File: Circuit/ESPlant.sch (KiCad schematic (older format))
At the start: 32 parts, among them P101 CONN_01X08, P102 CONN_01X08, P103 SOLAR, P104 USB_5PIN_SHELL, P105 CONN_01X05, Q101 FDN340P, SW101 RESET, SW102 PRGM, SW103 RESET, U101 STM32F042F, U102 ESP-12E

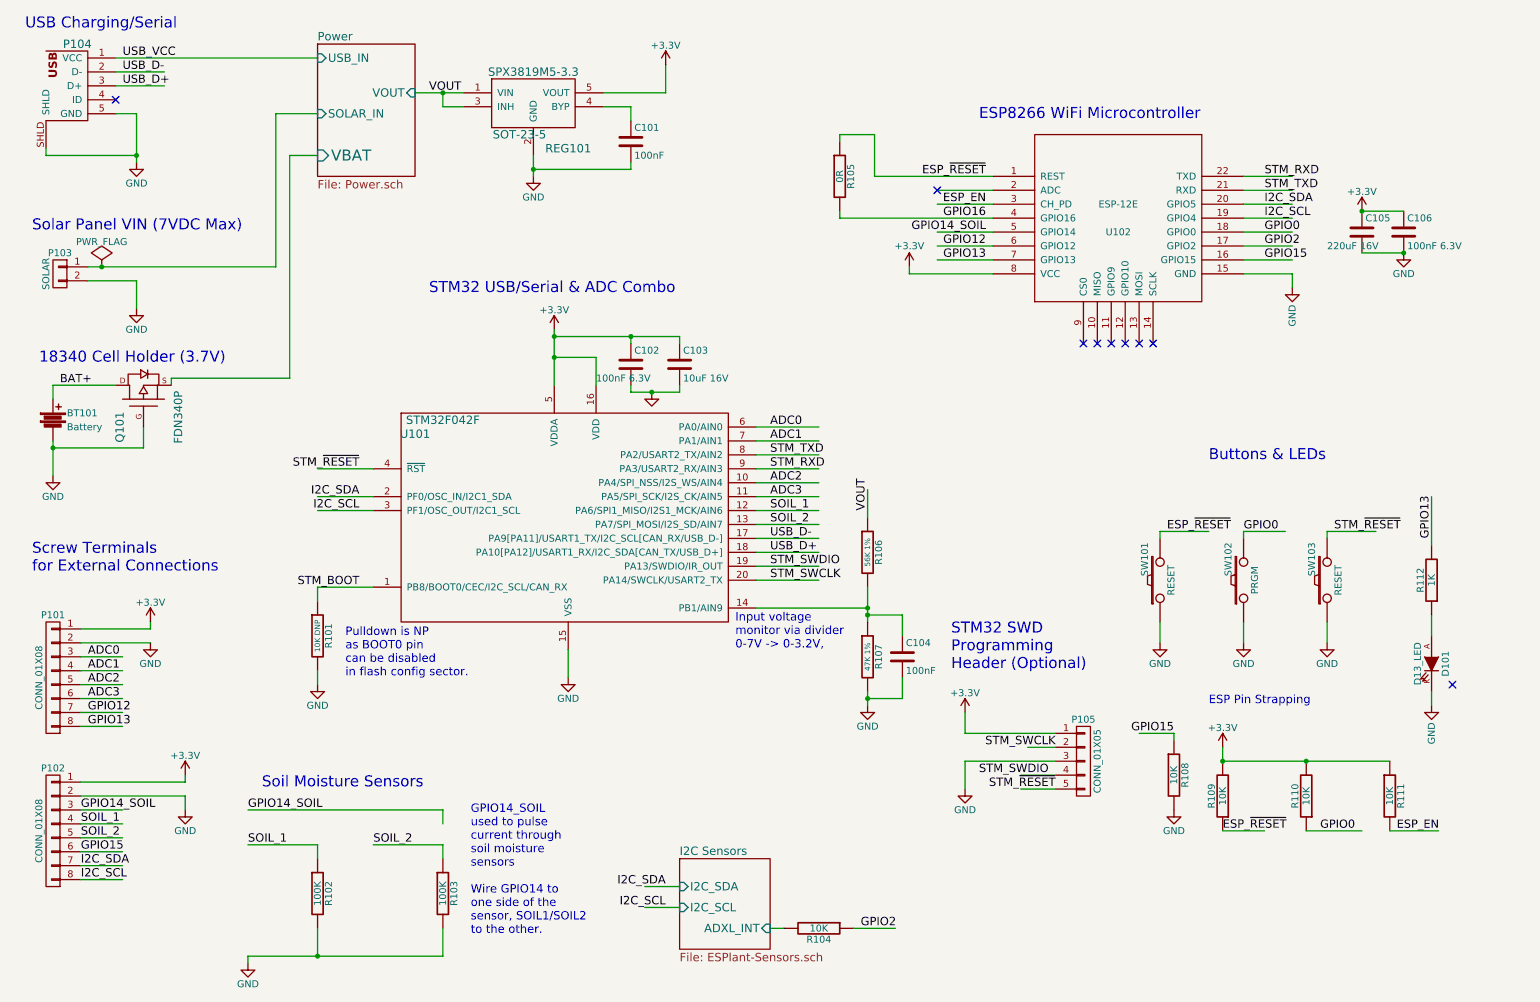
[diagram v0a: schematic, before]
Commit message: Schematic last touches
Added:
Breakouts for individual sensors.
Breakouts for all pins.
ESP controllable power.
Replaced Battery FET with Fuse.
Removed D13 LED.
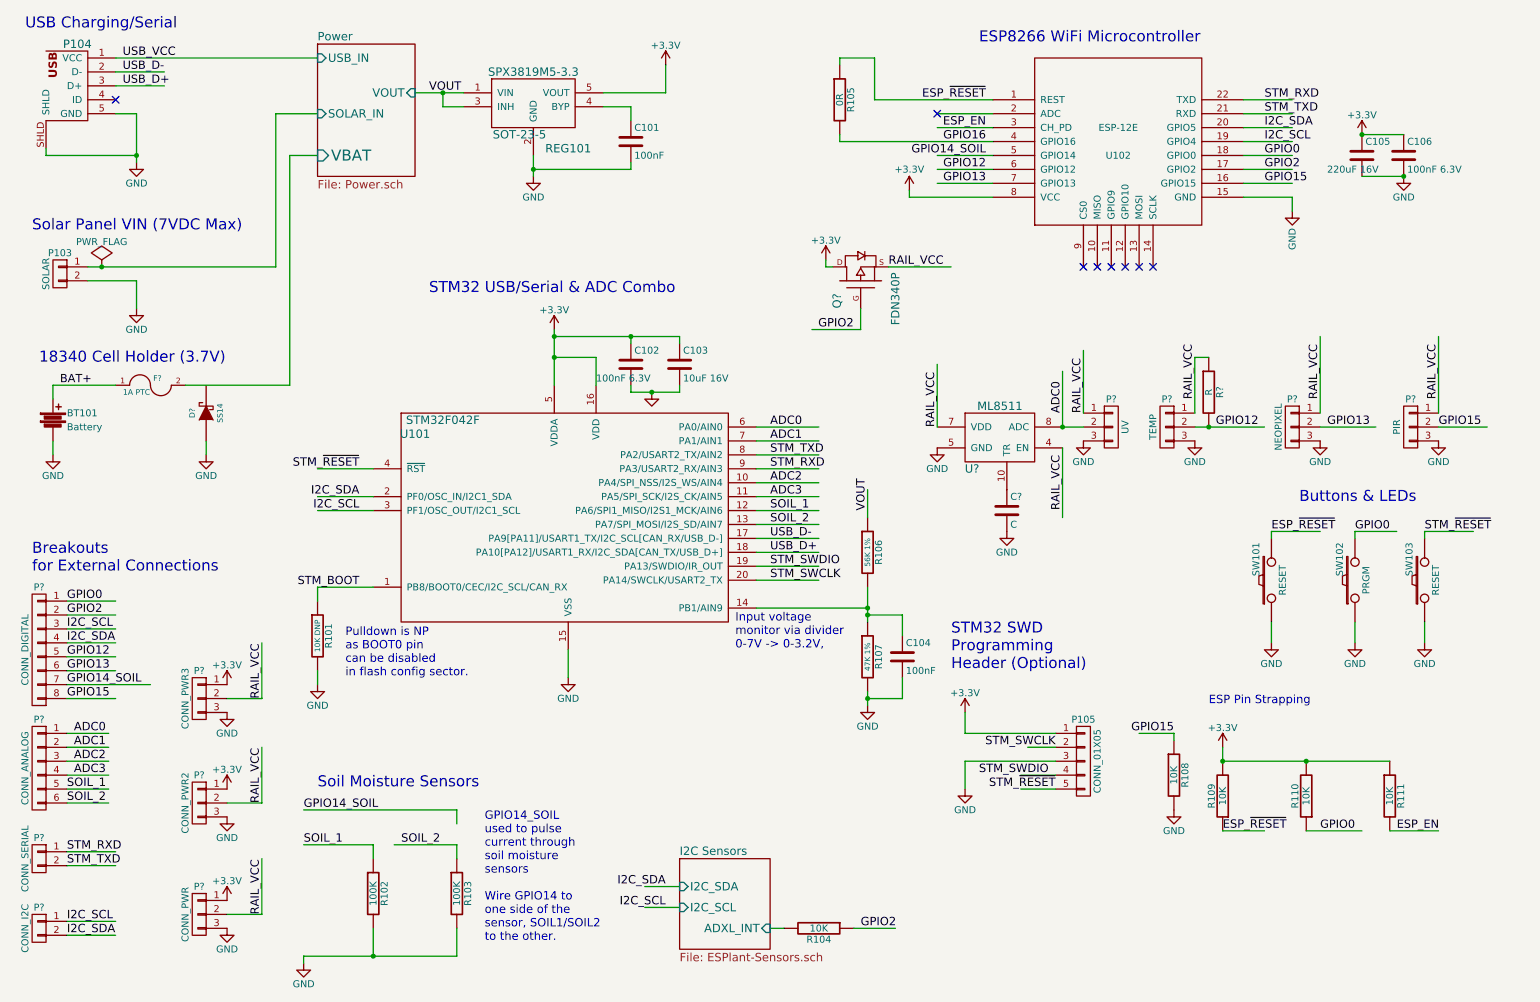
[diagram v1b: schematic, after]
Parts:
- removed D101: D13_LED, symbol LED
- removed P101, P102: CONN_01X08, symbol CONN_01X08
- removed Q101: FDN340P, symbol MOSFET_P
- removed R112: 1K, symbol R
- added C?: C, symbol C
- added D?: SS14, symbol DIODE_SCHOTTKY
- added F?: 1A PTC, symbol FUSE
- added P?: UV, symbol CONN_01X03
- added P?: PIR, symbol CONN_01X03
- added P?: TEMP, symbol CONN_01X03
- added P?: NEOPIXEL, symbol CONN_01X03
- added P?: CONN_PWR, symbol CONN_01X03
- added P?: CONN_ANALOG, symbol CONN_01X06
- added P?: CONN_SERIAL, symbol CONN_01X02
- added P?: CONN_DIGITAL, symbol CONN_01X08
- added P?: CONN_I2C, symbol CONN_01X02
- added P?: CONN_PWR3, symbol CONN_01X03
- added P?: CONN_PWR2, symbol CONN_01X03
- added Q?: FDN340P, symbol MOSFET_P
- added R?: R, symbol R
- added U?: ML8511, symbol ML8511
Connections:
- net labels added: RAIL_VCC
- wire segments 151 -> 168
- no-connect marks 9 -> 8
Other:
- note added: "Breakouts\nfor External Connections"
- note removed: "Screw Terminals\nfor External Connections"
- moved on the sheet: C105, C106, R102, R103, R105, SW101, SW102, SW103, U102

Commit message: Rename RAIL_VCC to VCC_SENS, add pullup and gate current resistor to FET
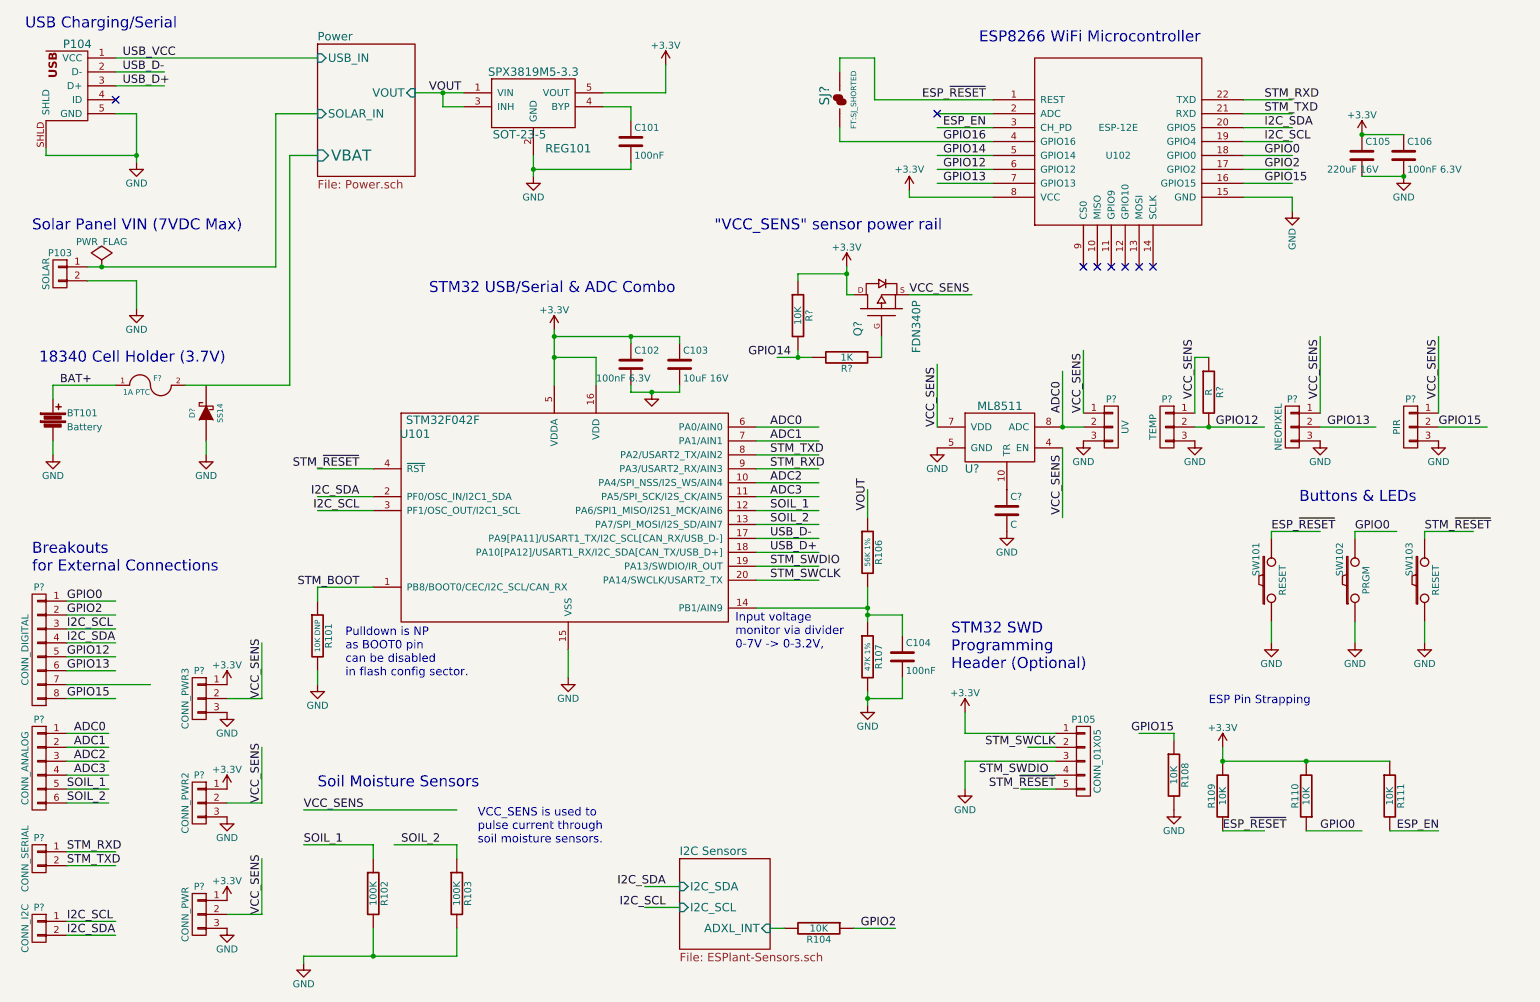
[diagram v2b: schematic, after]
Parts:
- removed R105: 0R, symbol R
- added R?: 10K, symbol R
- added R?: 1K, symbol R
- added SJ?: SJ, FT:SJ_SHORTED, symbol SJ
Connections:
- net labels added: GPIO14, VCC_SENS
- net labels removed: GPIO14_SOIL, RAIL_VCC
- wire segments 168 -> 169
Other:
- note added: ""VCC_SENS" sensor power rail"
- note added: "VCC_SENS is used to\npulse current through\nsoil moisture sensors."
- note removed: "GPIO14_SOIL\nused to pulse\ncurrent through\nsoil moisture\nsensors\n\nWire GPIO14 to\none side of the\nsensor, SOIL1/SOIL2\nto the other."
- moved on the sheet: Q?
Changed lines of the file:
@@
 NoConn ~ 8350 2350
 NoConn ~ 8250 2350
-Text Notes 3950 7200 0    60   ~ 0
-GPIO14_SOIL\nused to pulse\ncurrent through\nsoil moisture\nsensors\n\nWire GPIO14 to\none side of the\nsensor, SOIL1/SOIL2\nto the other.
+Text Notes 3900 6500 0    60   ~ 0
+VCC_SENS is used to\npulse current through\nsoil moisture sensors.
 Text Label 6000 3500 0    60   ~ 0
 ADC0
-$Comp
-L R R105
-U 1 1 564EAB03
-P 6500 1150
-F 0 "R105" V 6580 1150 50  0000 C CNN
-F 1 "0R" V 6500 1150 50  0000 C CNN
-F 2 "" H 6500 1150 60  0000 C CNN
-F 3 "" H 6500 1150 60  0000 C CNN
-	1    6500 1150
-	1    0    0    -1
-$EndComp
 Text Label 7550 1550 2    60   ~ 0
-GPIO14_SOIL
+GPIO14
 Text Label 2650 6250 0    60   ~ 0
-GPIO14_SOIL
+VCC_SENS
 $Comp
 L GND #PWR019
@@
 L MOSFET_P Q?
 U 1 1 565907EF
-P 6650 2450
-F 0 "Q?" H 6560 2620 60  0000 R CNN
-F 1 "FDN340P" H 6710 2200 60  0000 R CNN
-F 2 "" H 6650 2450 60  0000 C CNN
-F 3 "" H 6650 2450 60  0000 C CNN
-	1    6650 2450
+P 6800 2650
+F 0 "Q?" H 6710 2820 60  0000 R CNN
+F 1 "FDN340P" H 6860 2400 60  0000 R CNN
+F 2 "" H 6800 2650 60  0000 C CNN
+F 3 "" H 6800 2650 60  0000 C CNN
+	1    6800 2650
 	0    -1   -1   0
 $EndComp
@@
 L +3.3V #PWR?
 U 1 1 56596CF8
-P 6400 2300
-F 0 "#PWR?" H 6400 2150 50  0001 C CNN
-F 1 "+3.3V" H 6400 2440 50  0000 C CNN
-F 2 "" H 6400 2300 60  0000 C CNN
-F 3 "" H 6400 2300 60  0000 C CNN
-	1    6400 2300
-	1    0    0    -1
-$EndComp
-Text Label 6600 2800 2    60   ~ 0
-GPIO2
-Text Label 6850 2350 0    60   ~ 0
-RAIL_VCC
+P 6550 2350
+F 0 "#PWR?" H 6550 2200 50  0001 C CNN
+F 1 "+3.3V" H 6550 2490 50  0000 C CNN
+F 2 "" H 6550 2350 60  0000 C CNN
+F 3 "" H 6550 2350 60  0000 C CNN
+	1    6550 2350
+	1    0    0    -1
+$EndComp
+Text Label 7000 2550 0    60   ~ 0
+VCC_SENS
 Text Label 7200 3500 1    60   ~ 0
-RAIL_VCC
+VCC_SENS
 Text Label 8100 3700 3    60   ~ 0
-RAIL_VCC
+VCC_SENS
 Text Label 9050 3300 1    60   ~ 0
-RAIL_VCC
+VCC_SENS
 Text Label 8250 3400 1    60   ~ 0
-RAIL_VCC
+VCC_SENS
 Text Label 9950 3300 1    60   ~ 0
-RAIL_VCC
+VCC_SENS
 Text Label 10800 3300 1    60   ~ 0
-RAIL_VCC
+VCC_SENS
 Wire Wire Line
 	3750 6500 3300 6500
@@
 	7200 3500 7200 3050
 Wire Wire Line
-	6400 2350 6450 2350
-Wire Wire Line
-	6400 2300 6400 2350
-Wire Wire Line
-	6650 2800 6300 2800
-Wire Wire Line
-	6650 2650 6650 2800
-Wire Wire Line
-	6850 2350 7300 2350
+	6550 2550 6600 2550
+Wire Wire Line
+	6550 2350 6550 2550
+Wire Wire Line
+	6800 3000 6800 2850
+Wire Wire Line
+	7000 2550 7450 2550
 Wire Wire Line
 	9050 3500 9550 3500
@@
 	2650 6500 3150 6500
 Wire Wire Line
-	3750 6250 3750 6350
-Wire Wire Line
 	2650 6250 3750 6250
 Wire Wire Line
-	6750 1450 6750 1450
-Wire Wire Line
-	6500 1400 6500 1450
-Wire Wire Line
-	6500 850  6500 900
+	6500 1350 6500 1450
+Wire Wire Line
+	6500 850  6500 950
 Wire Wire Line
 	6750 850  6500 850
@@
 	10450 6400 10800 6400
 Connection ~ 9850 5900
-Wire Wire Line
-	6500 1450 7600 1450
 Wire Wire Line
 	7600 1650 7200 1650
@@
 Text Label 950  5150 0    60   ~ 0
 GPIO12
-Text Label 950  5350 0    60   ~ 0
-GPIO14_SOIL
 $Comp
 L CONN_01X03 P?
@@
 $EndComp
 Text Label 2350 7000 1    60   ~ 0
-RAIL_VCC
+VCC_SENS
 $Comp
 L CONN_01X06 P?
@@
 $EndComp
 Text Label 2350 5450 1    60   ~ 0
-RAIL_VCC
+VCC_SENS
 Wire Wire Line
 	2100 5450 2350 5450
@@
 $EndComp
 Text Label 2350 6200 1    60   ~ 0
-RAIL_VCC
+VCC_SENS
 Wire Wire Line
 	2100 6200 2350 6200
@@
 Wire Wire Line
 	1950 3600 1950 3700
+$Comp
+L SJ SJ?
+U 1 1 56581F55
+P 6500 1150
+F 0 "SJ?" H 6400 1000 70  0000 L BNN
+F 1 "SJ" H 6400 1200 30  0001 L BNN
+F 2 "FT:SJ_SHORTED" H 6500 1250 39  0000 C CNN
+F 3 "" H 6500 1150 60  0000 C CNN
+	1    6500 1150
+	0    1    1    0
+$EndComp
+Wire Wire Line
+	6500 1450 7600 1450
+Text Label 6150 3000 2    60   ~ 0
+GPIO14
+$Comp
+L R R?
+U 1 1 56584EA4
+P 6200 2700
+F 0 "R?" V 6280 2700 50  0000 C CNN
+F 1 "10K" V 6200 2700 50  0000 C CNN
+F 2 "" H 6200 2700 60  0000 C CNN
+F 3 "" H 6200 2700 60  0000 C CNN
+	1    6200 2700
+	1    0    0    -1
+$EndComp
+Connection ~ 6200 3000
+Wire Wire Line
+	6200 2400 6550 2400
+Connection ~ 6550 2400
+$Comp
+L R R?
+U 1 1 56585798
+P 6550 3000
+F 0 "R?" V 6630 3000 50  0000 C CNN
+F 1 "1K" V 6550 3000 50  0000 C CNN
+F 2 "" H 6550 3000 60  0000 C CNN
+F 3 "" H 6550 3000 60  0000 C CNN
+	1    6550 3000
+	0    1    1    0
+$EndComp
+Wire Wire Line
+	6050 3000 6300 3000
+Wire Wire Line
+	6200 3000 6200 2950
+Wire Wire Line
+	6200 2450 6200 2400
+Text Notes 5600 2100 0    79   ~ 0
+"VCC_SENS" sensor power rail
 $EndSCHEMATC

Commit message: Footprint assignment for schematic, including footprints for new parts
Removed on-PCB UV sensor in favour of offboard one.
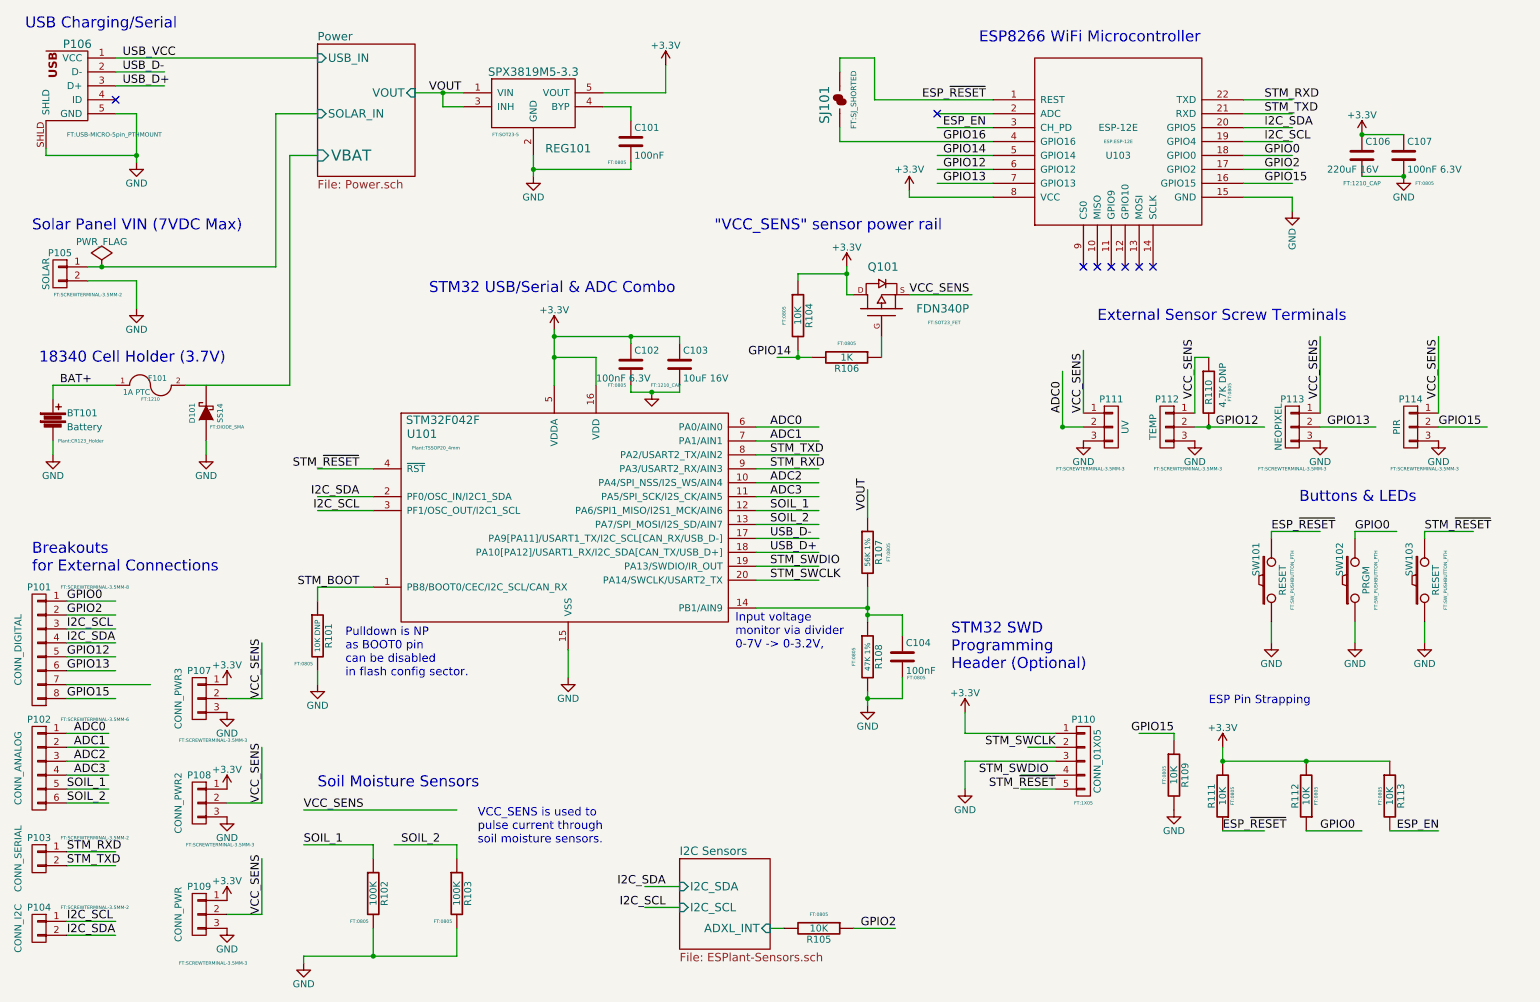
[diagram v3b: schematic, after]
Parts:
- removed C?: C, symbol C
- removed U?: ML8511, symbol ML8511
- BT101: footprint (none) -> Plant:CR123_Holder
- C101, C102, C104, R101, R102, R103: footprint (none) -> FT:0805
- C103: footprint (none) -> FT:1210_CAP
- C106: renamed from C105; footprint (none) -> FT:1210_CAP
- C107: renamed from C106; footprint (none) -> FT:0805
- D101: renamed from D?; footprint (none) -> FT:DIODE_SMA
- F101: renamed from F?; footprint (none) -> FT:1210
- P101: renamed from P?; footprint (none) -> FT:SCREWTERMINAL-3.5MM-8
- P102: renamed from P?; footprint (none) -> FT:SCREWTERMINAL-3.5MM-6
- P103, P104: renamed from P?; footprint (none) -> FT:SCREWTERMINAL-3.5MM-2
- P105: renamed from P103; footprint (none) -> FT:SCREWTERMINAL-3.5MM-2
- P106: renamed from P104; footprint FT:USB-MICRO_TH_4PEGS -> FT:USB-MICRO-5pin_PTHMOUNT
- P107, P108, P109, P111, P112, P113, P114: renamed from P?; footprint (none) -> FT:SCREWTERMINAL-3.5MM-3
- P110: renamed from P105; footprint (none) -> FT:1X05
- Q101: renamed from Q?; footprint (none) -> FT:SOT23_FET
- R104, R106: renamed from R?; footprint (none) -> FT:0805
- R105: renamed from R104; footprint (none) -> FT:0805
- R107: renamed from R106; footprint (none) -> FT:0805
- R108: renamed from R107; footprint (none) -> FT:0805
- R109: renamed from R108; footprint (none) -> FT:0805
- R110: renamed from R?; value R -> 4.7K DNP; footprint (none) -> FT:0805
- R111: renamed from R109; footprint (none) -> FT:0805
- R112: renamed from R110; footprint (none) -> FT:0805
- R113: renamed from R111; footprint (none) -> FT:0805
- REG101: footprint SOT-23-5 -> FT:SOT23-5
- SW101, SW102, SW103: footprint (none) -> FT:SW_PUSHBUTTON_PTH
- U101: footprint (none) -> Plant:TSSOP20_4mm
- U103: renamed from U102; footprint (none) -> ESP:ESP-12E
- gave numbers to parts that had none: 1
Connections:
- wire segments 169 -> 167
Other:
- note added: "External Sensor Screw Terminals"
